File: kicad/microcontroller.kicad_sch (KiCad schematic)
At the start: 3 parts, among them SW701 SW_Push, U701 STM32WB55RGVx

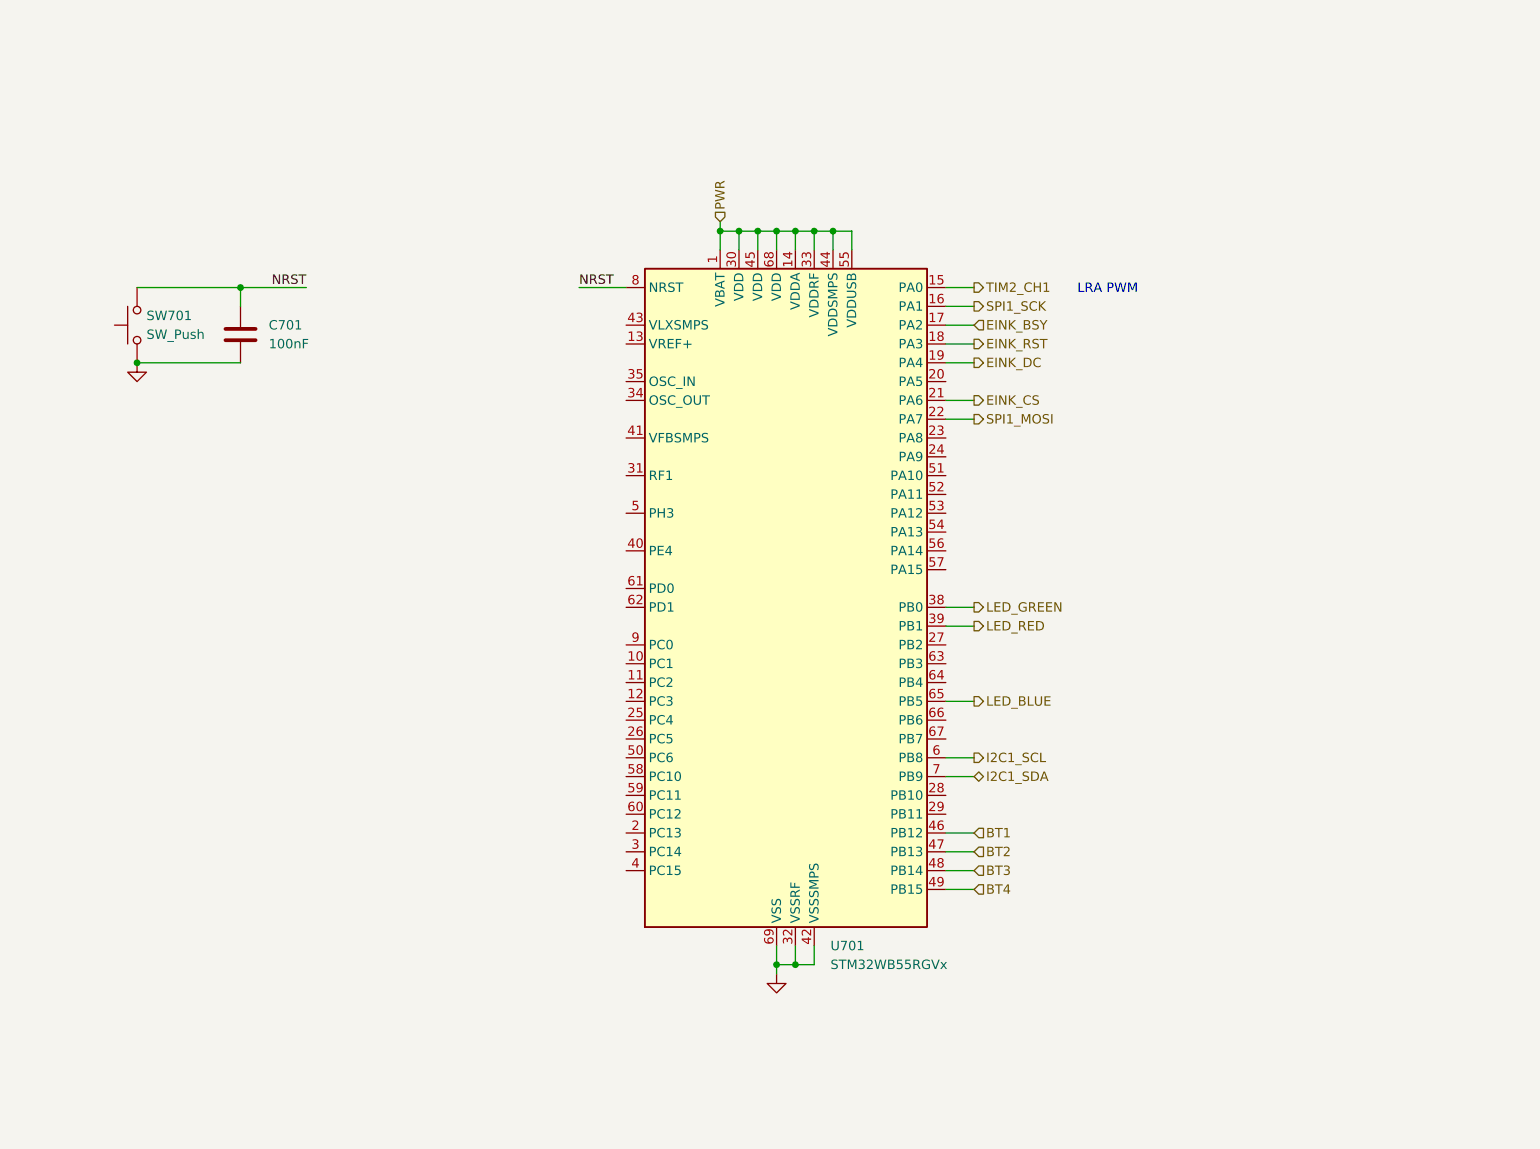
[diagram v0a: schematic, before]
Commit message: Start removing debug and integrate microcontroller
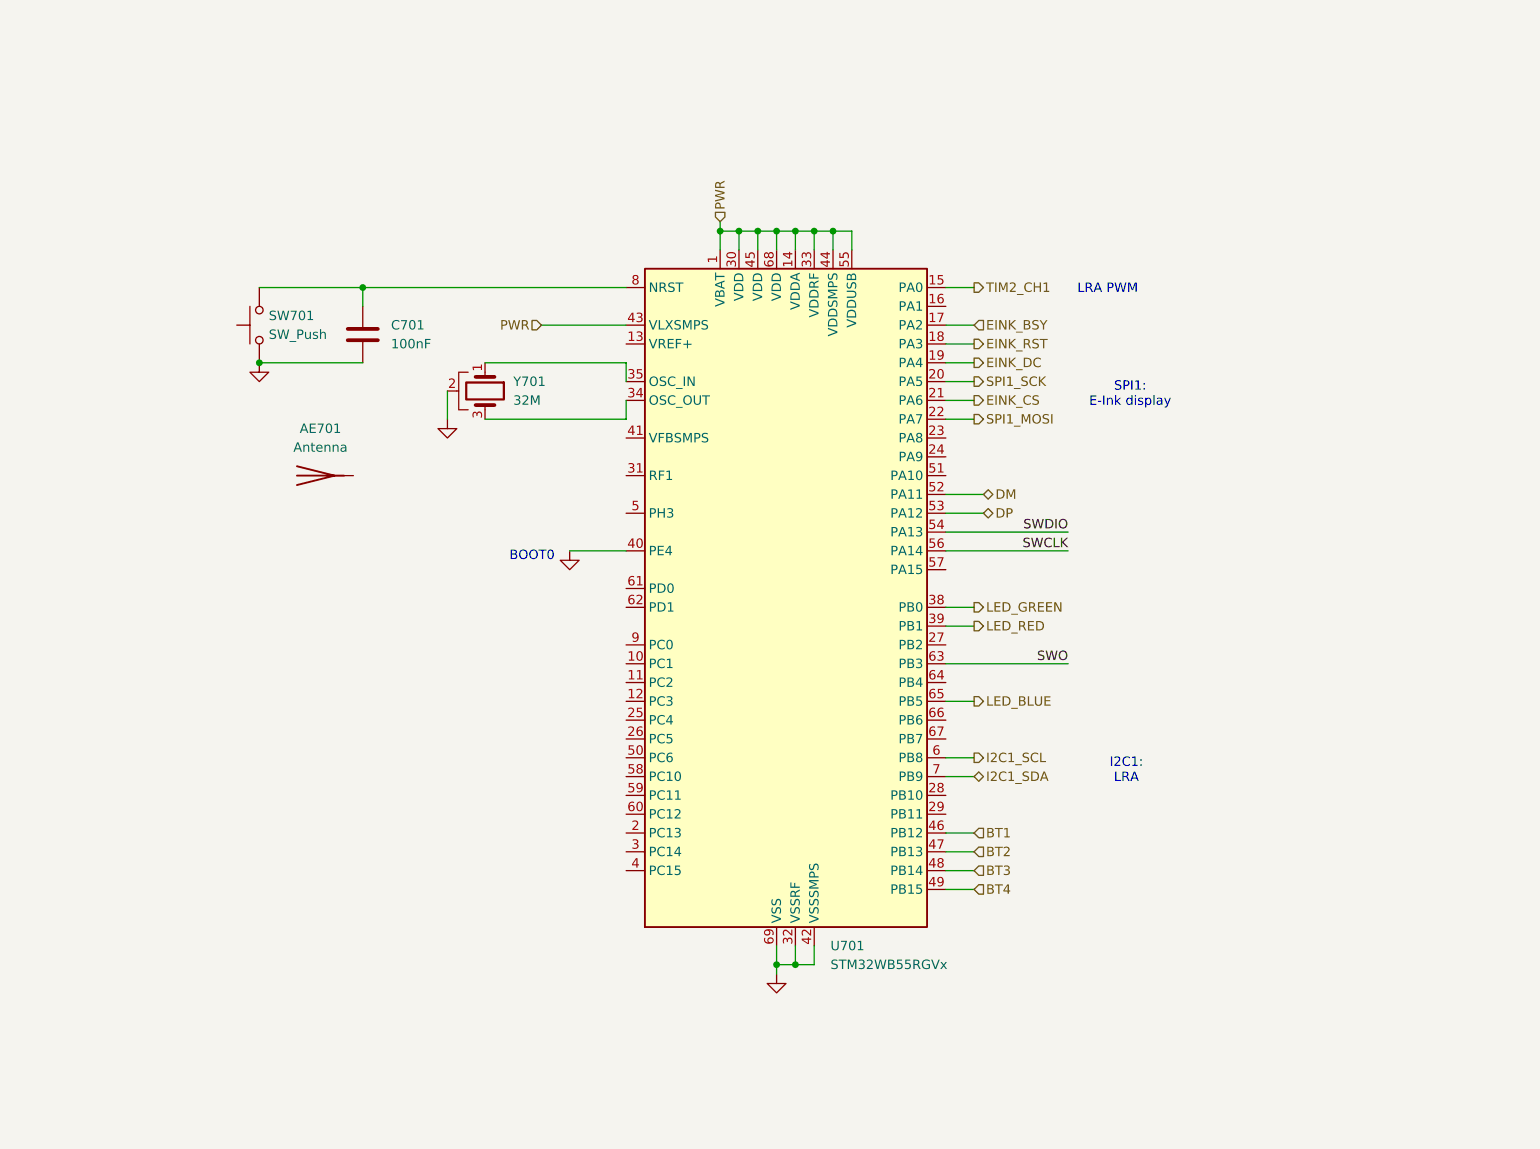
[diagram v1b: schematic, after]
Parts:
- added AE701: Antenna, symbol Device:Antenna
- added Y701: 32M, symbol Device:Crystal_GND2
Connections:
- net GND: now also U701.40 (PE4), Y701.2
- net PWR: now also U701.43 (VLXSMPS)
- net SPI1_SCK: now also U701.20 (PA5); no longer U701.16 (PA1)
- net at U701.34 (OSC_OUT): now also Y701.3
- net at U701.35 (OSC_IN): now also Y701.1
- net DM: now reaches U701.52 (PA11)
- net DP: now reaches U701.53 (PA12)
- net SWDIO: now reaches U701.54 (PA13)
- net SWCLK: now reaches U701.56 (PA14)
- net SWO: now reaches U701.63 (PB3)
- net NRST: no longer names the net of C701.1, SW701.2, U701.8 (NRST)
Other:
- note added: "BOOT0"
- note added: "I2C1: LRA"
- note added: "SPI1: E-Ink display"
- moved on the sheet: C701, SW701

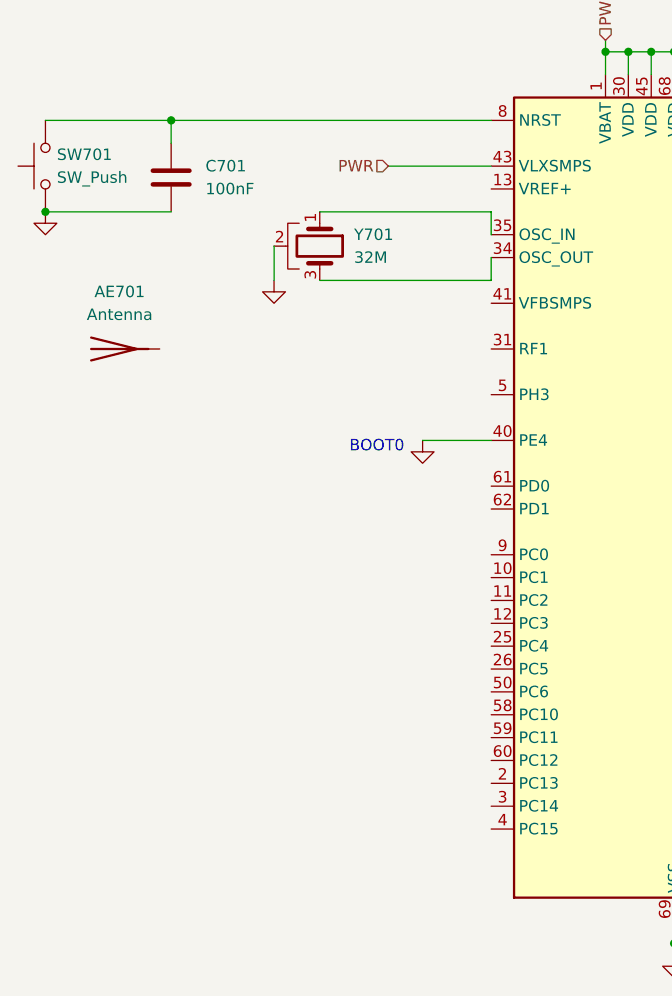
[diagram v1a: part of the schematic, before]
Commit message: Microcontroller additions
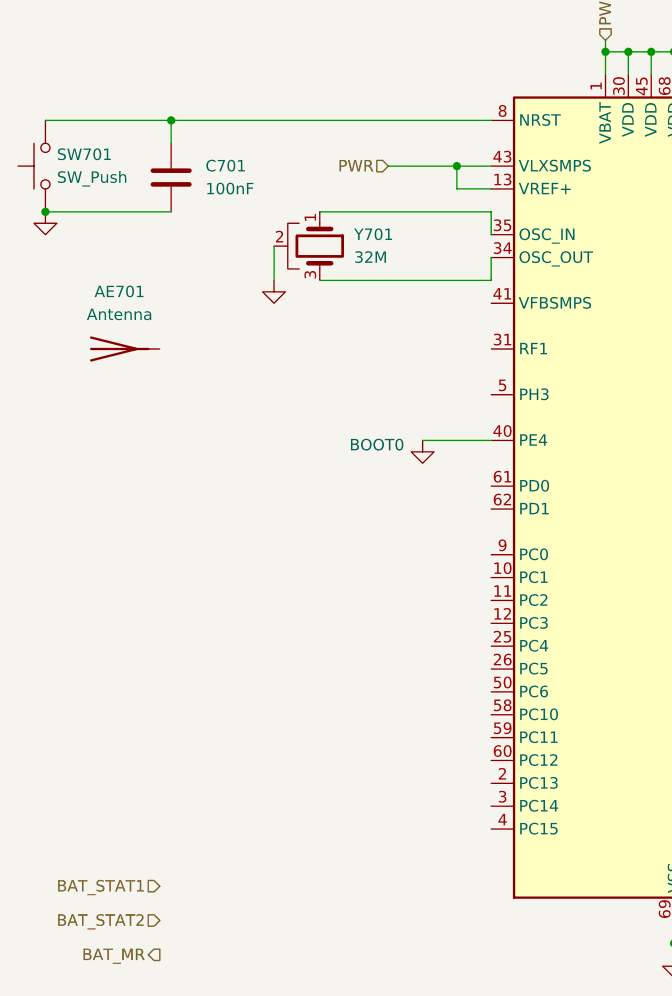
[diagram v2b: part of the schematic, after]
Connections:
- net PWR: now also U701.13 (VREF+)
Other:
- company: (none) -> Mosaic Labs
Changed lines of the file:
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@@
 		(date "2025-01-27")
 		(rev "1")
+		(company "Mosaic Labs")
+		(comment 1 "Lucas Merritt")
 	)
 	(junction
@@
 	)
 	(junction
+		(at 99.06 59.69)
+		(diameter 0)
+		(color 0 0 0 0)
+	)
+	(junction
 		(at 115.57 46.99)
 		(diameter 0)
@@
 	(wire
 		(pts
-			(xy 91.44 59.69) (xy 102.87 59.69)
+			(xy 91.44 59.69) (xy 99.06 59.69)
+		)
+		(stroke
+			(width 0)
+			(type default)
+		)
+	)
+	(wire
+		(pts
+			(xy 99.06 59.69) (xy 102.87 59.69)
 		)
 		(stroke
@@
 	(wire
 		(pts
+			(xy 99.06 62.23) (xy 99.06 59.69)
+		)
+		(stroke
+			(width 0)
+			(type default)
+		)
+	)
+	(wire
+		(pts
 			(xy 95.25 90.17) (xy 102.87 90.17)
 		)
@@
 		(pts
 			(xy 146.05 100.33) (xy 149.86 100.33)
+		)
+		(stroke
+			(width 0)
+			(type default)
+		)
+	)
+	(wire
+		(pts
+			(xy 102.87 62.23) (xy 99.06 62.23)
 		)
 		(stroke
@@
 		)
 	)
+	(hierarchical_label "BAT_STAT1"
+		(shape input)
+		(at 66.04 139.7 180)
+		(fields_autoplaced yes)
+		(effects
+			(font
+				(size 1.27 1.27)
+			)
+			(justify right)
+		)
+	)
 	(hierarchical_label "DP"
 		(shape bidirectional)
@@
 		)
 	)
+	(hierarchical_label "BAT_STAT2"
+		(shape input)
+		(at 66.04 143.51 180)
+		(fields_autoplaced yes)
+		(effects
+			(font
+				(size 1.27 1.27)
+			)
+			(justify right)
+		)
+	)
 	(hierarchical_label "TIM2_CH1"
 		(shape output)
@@
 		)
 	)
+	(hierarchical_label "BAT_MR"
+		(shape output)
+		(at 66.04 147.32 180)
+		(fields_autoplaced yes)
+		(effects
+			(font
+				(size 1.27 1.27)
+			)
+			(justify right)
+		)
+	)

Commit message: Unfinished switch additions and fixes
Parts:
- removed AE701: Antenna, symbol Device:Antenna
- removed C701: 100nF, symbol Device:C
- removed SW701: SW_Push, symbol Switch:SW_Push
- added Q701: 2N7002, Package_TO_SOT_SMD:SOT-23-3, symbol Simulation_SPICE:NMOS
- added R701: 100k, Resistor_SMD:R_0603_1608Metric_Pad0.98x0.95mm_HandSolder, symbol Device:R
- added R702: 10k, symbol Device:R
- added TP701: NRST_PAD, symbol Connector:TestPoint
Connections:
- net BT1: now also Q701.2 (G), R701.1
- net GND: now also Q701.3 (S), R701.2; no longer U701.40 (PE4)
- net PWR: now also R702.1
- net at U701.8 (NRST): now also TP701.1
- new net: Q701.1 (D), R702.2, U701.40 (PE4)
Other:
- note added: "As we can handle reset through power switch, just expose through pad"
- note added: "If BT1 held on power on, trigger bootloader for USB DFU"

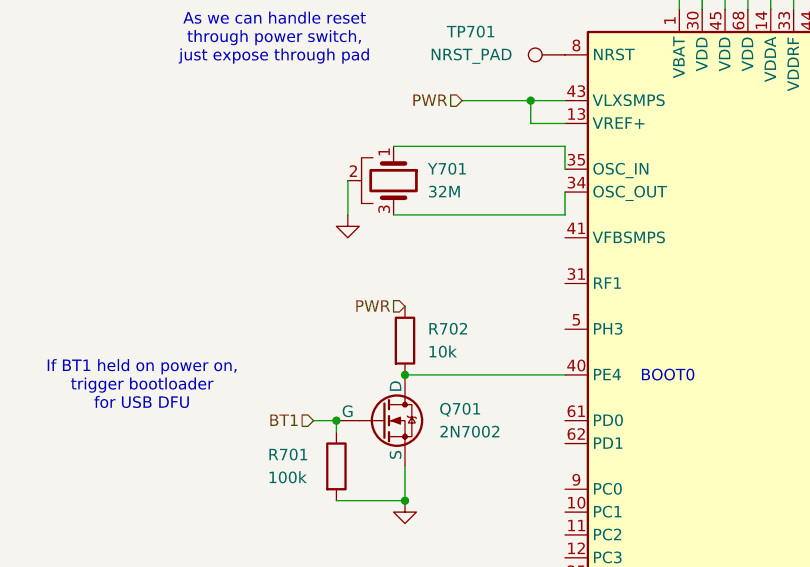
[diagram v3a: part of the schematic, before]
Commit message: Small switch updates and fixes
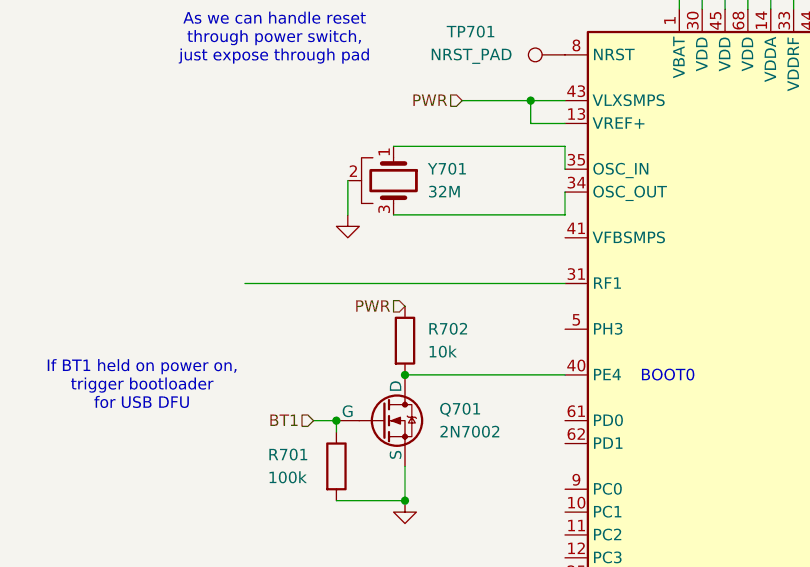
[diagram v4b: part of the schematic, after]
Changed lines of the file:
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@@
+	(wire
+		(pts
+			(xy 67.31 80.01) (xy 102.87 80.01)
+		)
+		(stroke
+			(width 0)
+			(type default)
+		)
+	)
 	(wire
 		(pts
@@
 		(dnp no)
 		(fields_autoplaced yes)
-		(property "Reference" "#PWR0701"
+		(property "Reference" "#PWR0703"
 			(at 123.19 153.67 0)
 			(effects
@@
 			(project "kicad"
 				(path "/97e37379-fec6-4f0d-82d9-4ea53516bb02/99a09460-9ccb-48eb-a131-ff3ce53fbef9"
-					(reference "#PWR0701")
+					(reference "#PWR0703")
 					(unit 1)
 				)
@@
 		(dnp no)
 		(fields_autoplaced yes)
-		(property "Reference" "#PWR0703"
+		(property "Reference" "#PWR0701"
 			(at 78.74 78.74 0)
 			(effects
@@
 			(project "kicad"
 				(path "/97e37379-fec6-4f0d-82d9-4ea53516bb02/99a09460-9ccb-48eb-a131-ff3ce53fbef9"
-					(reference "#PWR0703")
+					(reference "#PWR0701")
 					(unit 1)
 				)

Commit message: Part updates
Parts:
- added C701: 100pF, symbol Device:C
- added C702, C703, C704, C705, C706: 100nF, symbol Device:C
- R702: footprint (none) -> Resistor_SMD:R_0603_1608Metric_Pad0.98x0.95mm_HandSolder
- TP701: footprint (none) -> TestPoint:TestPoint_Pad_D1.0mm
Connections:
- net GND: now also C701.2, C702.2, C703.2, C704.2, C705.2, C706.2; no longer R701.2
- net PWR: now also C701.1, C702.1, C703.1, C704.1, C705.1, C706.1; no longer U701.1 (VBAT), U701.13 (VREF+), U701.14 (VDDA), U701.43 (VLXSMPS), U701.44 (VDDSMPS), U701.55 (VDDUSB)
- new net VDDA: U701.14 (VDDA)
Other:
- moved on the sheet: Q701, R701, R702, TP701, U701, Y701
